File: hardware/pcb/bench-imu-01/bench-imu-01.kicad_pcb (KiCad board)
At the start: 4 copper layers, 150 x 95 mm, 53 parts, among them J1 USB_C_Receptacle_GCT_USB4105-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, J2 PinHeader_1x04_P2.54mm_Vertic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, J3 PinHeader_1x04_P2.54mm_Vertic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, J4 BarrelJack_CUI_PJ-102AH_Horiz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, M1 TerminalBlock_MaiXu_MX126-5.0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, SW1 SW_PUSH_6mm, U1 LQFP-32_7x7mm_P0.8mm, U2 Bosch_LGA-14_3x2.5mm_P0.5mm, U3 SOT-23-5, U4 SOT-23-6, U5 HTSSOP-24-1EP_4.4x7.8mm_P0.65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, U6 HTSSOP-20-1EP_4.4x6.5mm_P0.65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

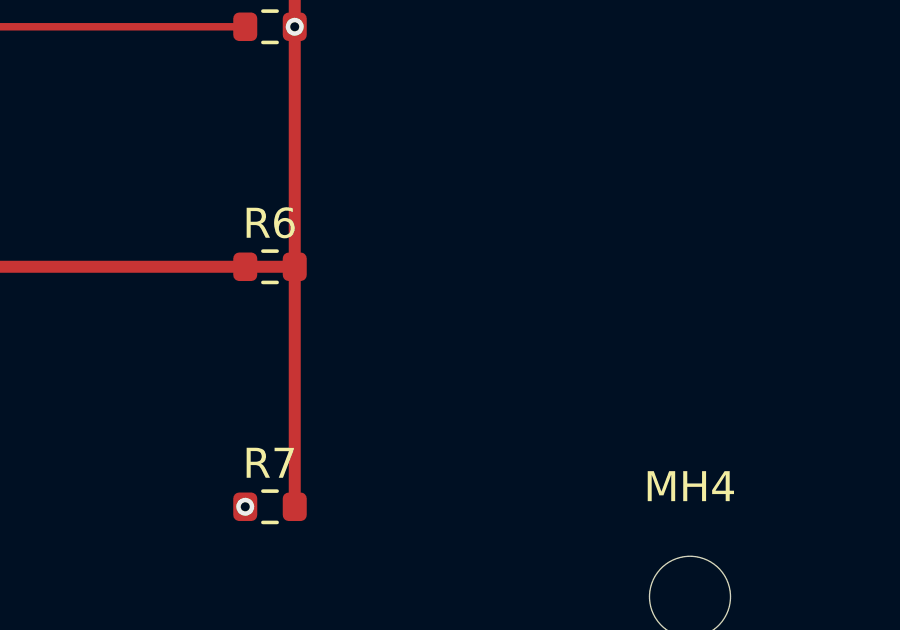
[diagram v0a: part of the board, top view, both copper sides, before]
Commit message: Bench-IMU-01: add GitHub logo + @ktanino10 attribution to PCB silkscreen
Add a small, purely decorative GitHub "Invertocat" logo plus the
designer's own GitHub handle (@ktanino10) to the front silkscreen of
hardware/pcb/bench-imu-01/bench-imu-01.kicad_pcb, per Kyosuke's direct
request. One new graphical footprint, "Logo_GitHub_ktanino10", at
(134.0, 76.0) mm on F.SilkS: 93 run-length-merged fp_rect fills (a
64x64 monochrome downsample of the official GitHub-Mark asset from
github.githubassets.com) plus one fp_text reading "@ktanino10". Carries
(attr exclude_from_pos_files exclude_from_bom allow_missing_courtyard)
-- zero pads, zero nets, not part of the BOM or pick-and-place file.

Brand-guideline reasoning: small, secondary-placement use paired with
the account holder's own handle on a personal, non-commercial hobby
PCB matches GitHub's own published "social button" allowance
(github.com/logos), not the prohibited "imply affiliation" / "use as
your own logo" cases.

Independently re-verified (not just relayed from the prior session
that prepared the ready-to-splice fragment):
- kicad-cli pcb export svg/pdf both succeed against the modified board
  -- confirms the file still parses correctly.
- kicad-cli pcb drc re-run 5x on the unmodified baseline (358, 360,
  363, 374, 358 violations) and 5x on the modified board (369, 355,
  363, 372, 366) -- fully overlapping bands, identical violation-type
  composition each time, and zero violations reference the new
  footprint in any of the 5 modified-board DRC JSON reports.
- A rendered silkscreen view confirms the mark sits in empty board
  space, clear of the R6/R7/R9/R10 resistor column and the MH4
  mounting hole.

Documentation judgement call: not an ECO. hardware-design.instructions
.md only requires a validation/change-log.md entry for a *non-cosmetic*
change to hardware/**/bom/** -- this has no net, pad, BOM line, or
footprint standing in for a real component, and measurably zero DRC
impact. Not an open-issues.md en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
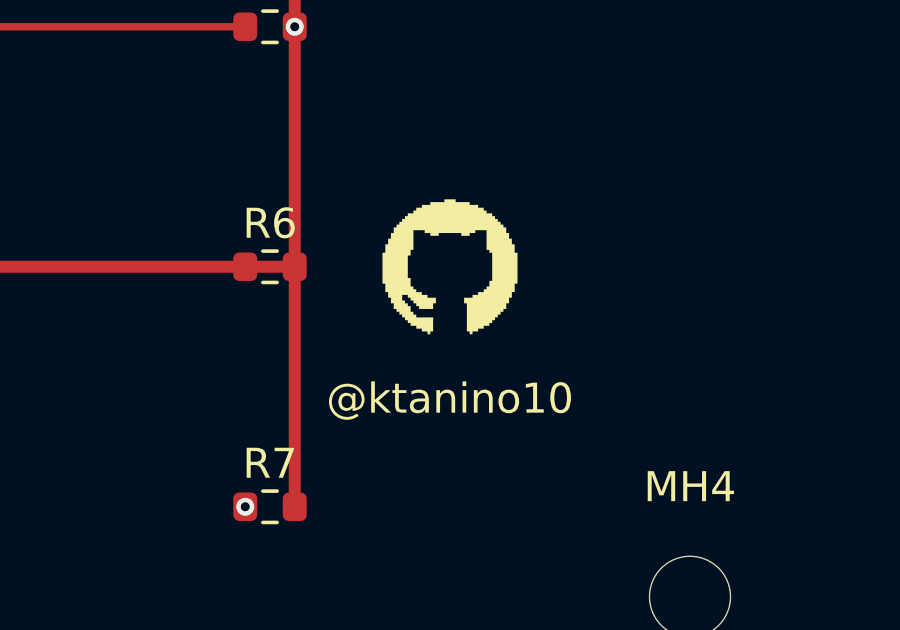
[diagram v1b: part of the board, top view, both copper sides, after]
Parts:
- added ?: , Logo_GitHub_ktanino10, F.Cu at (134.0, 76.0)

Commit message: Bench-IMU-01: enlarge + reposition GitHub logo silkscreen mark (upper-right)
Follow-up to PR #30 (merged). The human reviewed the rendered result and
asked for the small decorative GitHub logo + @ktanino10 silkscreen mark to
be moved and made bigger:

- Size: 6mm -> 12mm (logo), 1mm -> 1.5mm font (handle text).
- Position: (134, 76) bottom-right near MH4 -> (131, 20) upper-right, in
  the clear gap between the D2/D3/F1 protection-circuit cluster and MH2.

Everything else about the footprint (93 run-length-merged fp_rect
silkscreen fills + one fp_text, exclude_from_pos_files/exclude_from_bom/
allow_missing_courtyard, zero pads/nets) is unchanged from what PR #30
already established and justified in docs/architecture-evolution.md #40 --
this is a cosmetic resize/reposition only, not a new design decision.

Independent re-verification performed in this session (not just trusting
the pre-derived fragment):
- Checked upper-right quadrant component positions on the real board
  (MH2, D2/D3, capacitor, F1, three 0603 resistors) before confirming the
  new spot is clear on every side.
- Ran kicad-cli pcb drc --format json --severity-all 3 times: 373/363/368
  total violations, within this board's long-documented run-to-run DRC
  noise band (358-374, see #40). Zero silk_over_copper violations in all
  3 runs, and zero violations reference the logo footprint at all.
- Rendered in 3D (kicad-cli pcb render) and exported 2D SVG
  (kicad-cli pcb export svg, F.SilkS+F.Cu+Edge.Cuts) as two independent
  pipelines -- both confirm the enlarged mark sits cleanly in the gap with
  no overlap of D2/D3/F1/MH2/the R-row, and match the parent session's
  supplied verification render in composition.

Also corrected docs/architecture-evolution.md #40, which cited the old
PR #30 coordinates/clearance description as current fact:
- "board position (134.0, 76.0) mm" -> "(131.0, 20.0) mm"
- "clear of the R6/R7/R9/R10 resistor column and the MH4 mounting hole"
  -> "clear of the D2/D3/F1 protecti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
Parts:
- moved ? 56.1 mm to (131.0, 20.0)
